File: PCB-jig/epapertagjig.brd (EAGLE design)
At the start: 100 x 81.3 mm, 48 parts, among them J1 CORTEX_JTAG_DEBUG_PTH, J10 CORTEX_JTAG_DEBUG_PTH, J4 CORTEX_JTAG_DEBUG_PTH, J6 JTAG, J7 CORTEX_JTAG_DEBUG_PTH, J9 ESP32-S3_DEVKITC-1, Q1 1.1A/60V/600mΩ, Q2 5.8A/30V/35mΩ, Q3 1.1A/60V/600mΩ, Q4 5.8A/30V/35mΩ

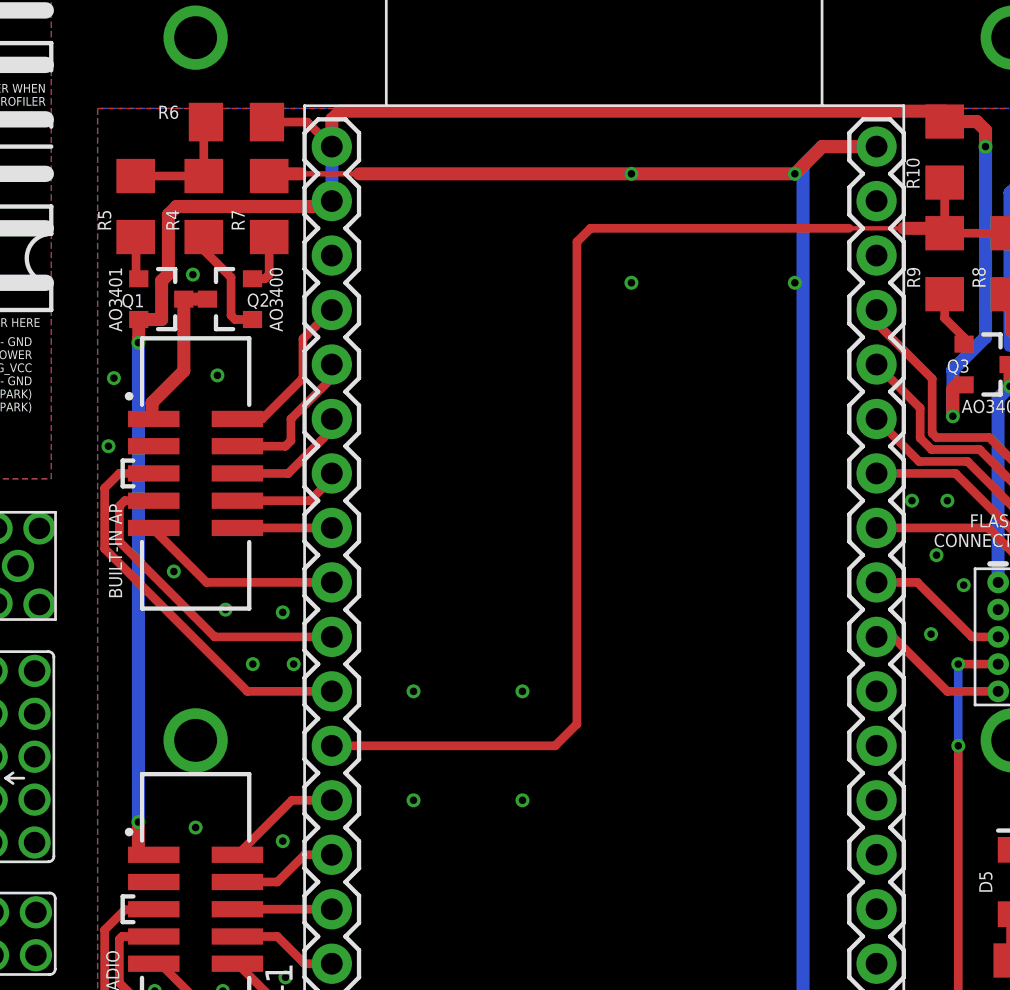
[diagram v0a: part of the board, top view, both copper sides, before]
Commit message: fixed mistake in PCB
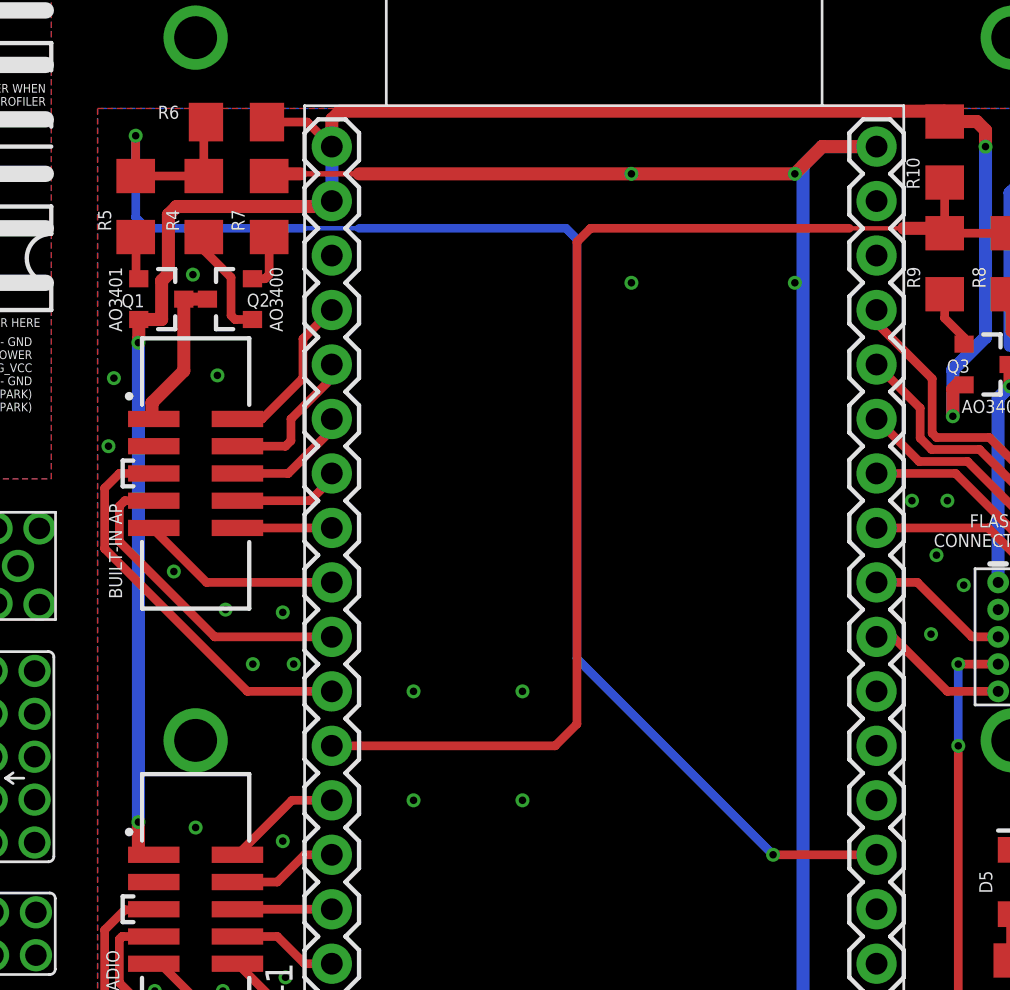
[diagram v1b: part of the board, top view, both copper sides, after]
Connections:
- net N$41: now also J9.0
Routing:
- net N$41: track 5.79 -> 69.8 mm, vias 0 -> 2
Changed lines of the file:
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@@
 <wire x1="57.912" y1="70.383" x2="57.912" y2="72.898" width="0.4064" layer="1"/>
 <wire x1="57.912" y1="72.898" x2="58.014" y2="72.898" width="0.4064" layer="1"/>
+<contactref element="J9" pad="0"/>
+<wire x1="54.737" y1="70.383" x2="54.737" y2="72.263" width="0.4064" layer="1"/>
+<via x="54.737" y="72.263" extent="1-16" drill="0.35"/>
+<wire x1="54.737" y1="72.263" x2="54.737" y2="68.453" width="0.4064" layer="16"/>
+<wire x1="54.737" y1="68.453" x2="55.245" y2="67.945" width="0.4064" layer="16"/>
+<wire x1="55.245" y1="67.945" x2="62.5348" y2="67.945" width="0.4064" layer="16"/>
+<wire x1="62.5348" y1="67.945" x2="65.151" y2="67.945" width="0.2032" layer="16"/>
+<wire x1="65.151" y1="67.945" x2="74.803" y2="67.945" width="0.4064" layer="16"/>
+<wire x1="74.803" y1="67.945" x2="75.311" y2="67.437" width="0.4064" layer="16"/>
+<wire x1="75.311" y1="67.437" x2="75.311" y2="47.879" width="0.4064" layer="16"/>
+<wire x1="75.311" y1="47.879" x2="84.455" y2="38.735" width="0.4064" layer="16"/>
+<via x="84.455" y="38.735" extent="1-16" drill="0.35"/>
+<wire x1="84.455" y1="38.735" x2="89.281" y2="38.735" width="0.4064" layer="1"/>
 </signal>
 <signal name="N$42">
